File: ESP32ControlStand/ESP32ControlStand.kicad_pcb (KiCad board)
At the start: 2 copper layers, 184.1 x 144.1 mm, 118 parts, among them CON101 BARREL_JACK, J101 Button & LED Panel, J102 Horn, J103 Brake, J104 I2C Display, J105 Button & LED Panel, J106 Light Switch, J107 Reverser, J108 Throttle, J109 On-Off Switch, J401 RJ45, J402 RJ45, P101 CONN_8, P102 Misc buttons, bell, status LED, P106 CONN_3, P107 CONN_3, P201 CONN_5, P301 CONN_5, SW101 A, SW102 B, SW103 C, SW104 D, SW105 Bell, SW201 SW_PUSH_SMALL, SW202 SW_PUSH_SMALL, SW203 SW_PUSH_SMALL, SW204 SW_PUSH_SMALL, SW205 SW_PUSH_SMALL, SW206 SW_PUSH_SMALL, SW207 SW_PUSH_SMALL, SW208 SW_PUSH_SMALL, SW301 SW_PUSH_SMALL, SW302 SW_PUSH_SMALL, SW303 SW_PUSH_SMALL, SW304 SW_PUSH_SMALL, SW305 SW_PUSH_SMALL, SW306 SW_PUSH_SMALL, SW307 SW_PUSH_SMALL, SW308 SW_PUSH_SMALL, T201 Buttons, T202 LEDS, T301 Buttons, T302 LEDS, T401 + 15 in -, T402 + 15 out -, U101 ADAFRUIT_POWERBOOST_500, U102 TTGO-T1, U201 MCP23017, U202 TBD62083A, U301 MCP23017, U302 TBD62083A, U401 TCAN332DR, U402 SN65HVD233-HT, U501 LM2574N-5.0

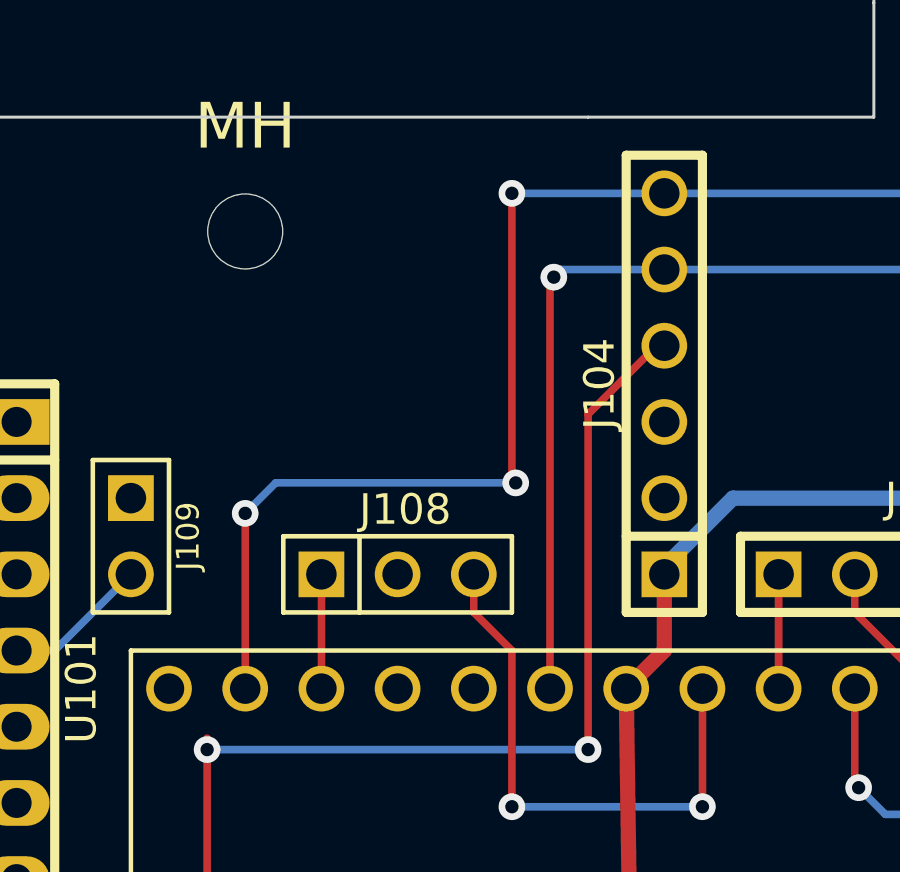
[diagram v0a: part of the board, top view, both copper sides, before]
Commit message: Update circuit to use "Default" SDA/SDL.
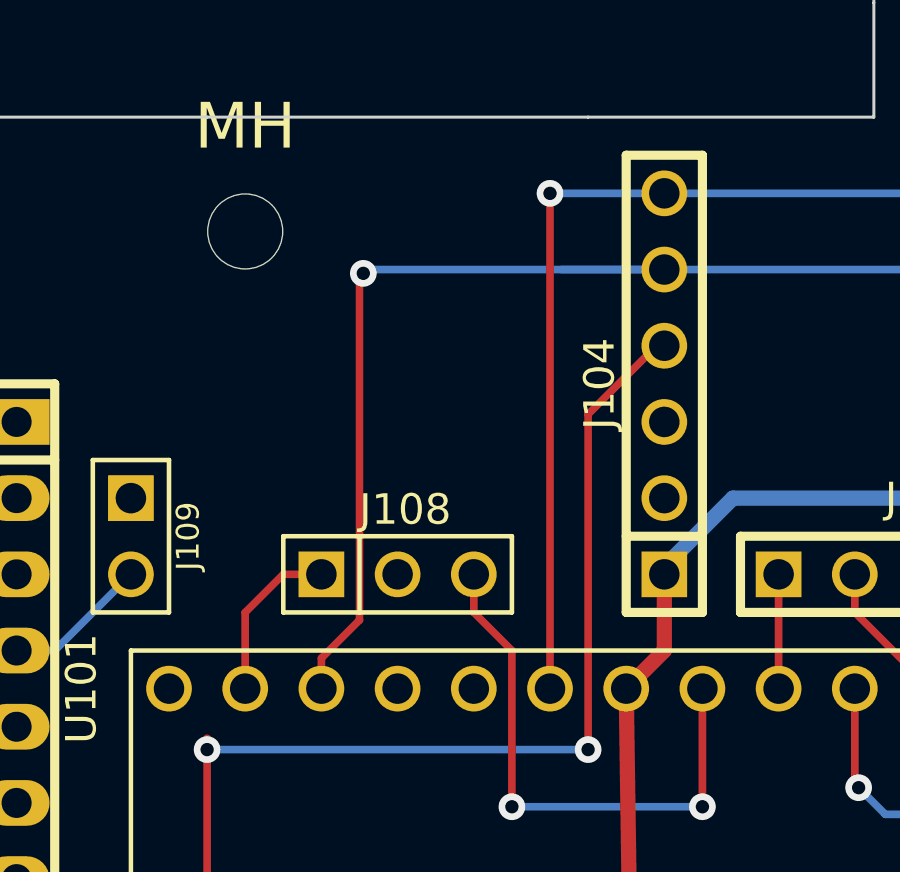
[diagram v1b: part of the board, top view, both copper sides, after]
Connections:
- U102 pad 31: /SCL -> /SDA
- U102 pad 34: /ThrottleA -> /SCL
- U102 pad 35: /SDA -> /ThrottleA
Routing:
- net /SCL: track 42.0 -> 52.1 mm
- net /SDA: track 54.2 -> 44.5 mm, vias 3 -> 1
- net /ThrottleA: track 3.81 -> 5.61 mm

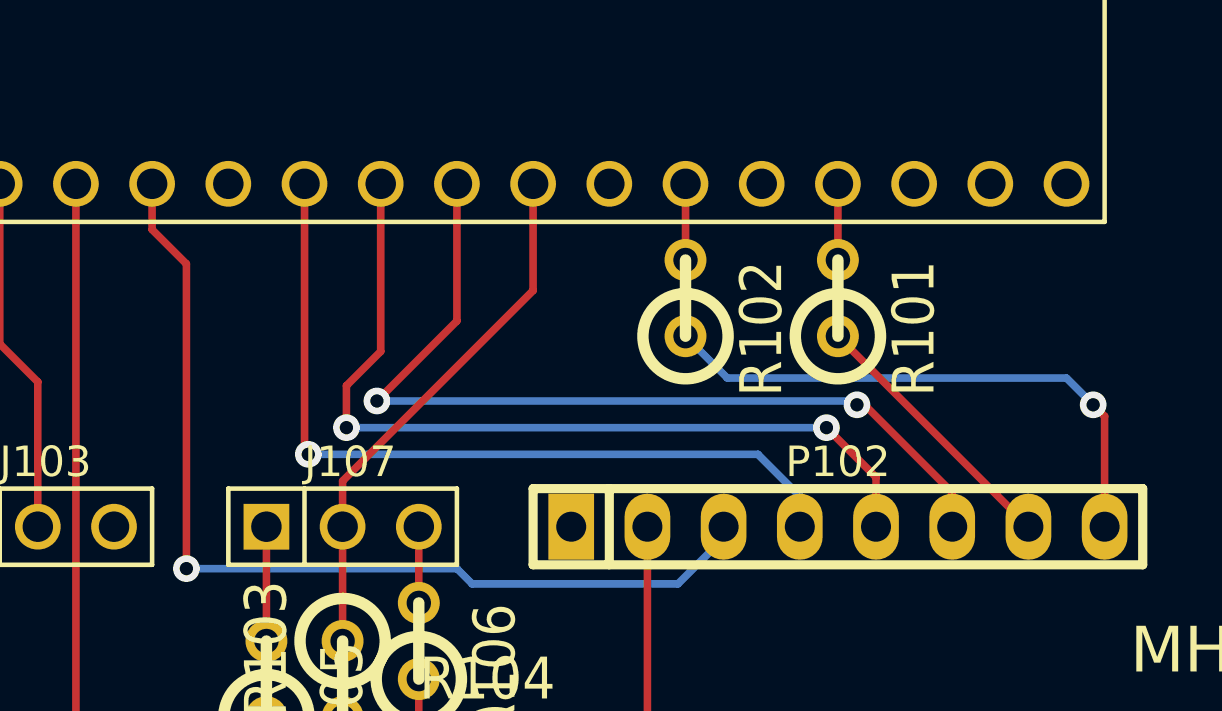
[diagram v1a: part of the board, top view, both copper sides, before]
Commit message: Fix I/O conflict (Status_G).
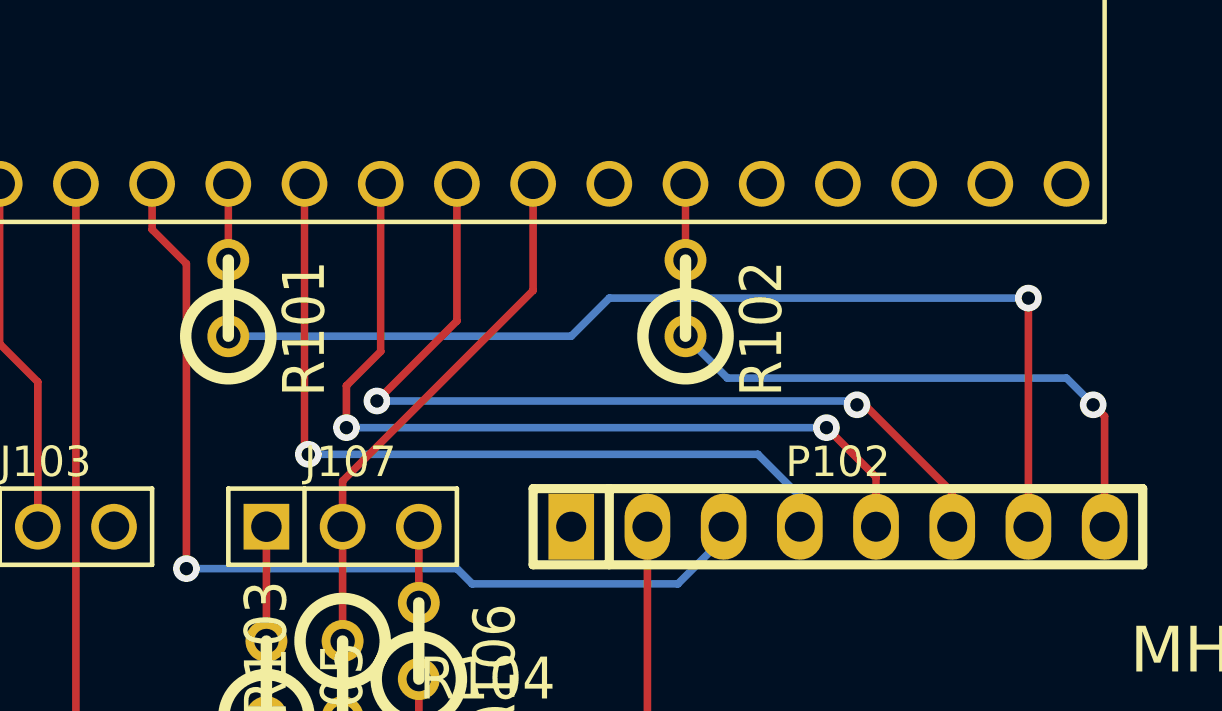
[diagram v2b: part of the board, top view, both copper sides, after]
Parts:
- moved R101 20.3 mm to (191.8, 210.8)
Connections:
- U102 pad 15: /Status_G -> (no net)
- U102 pad 7: (no net) -> /Status_G
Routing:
- net N-0000035: track 8.98 -> 34.8 mm, vias 0 -> 1

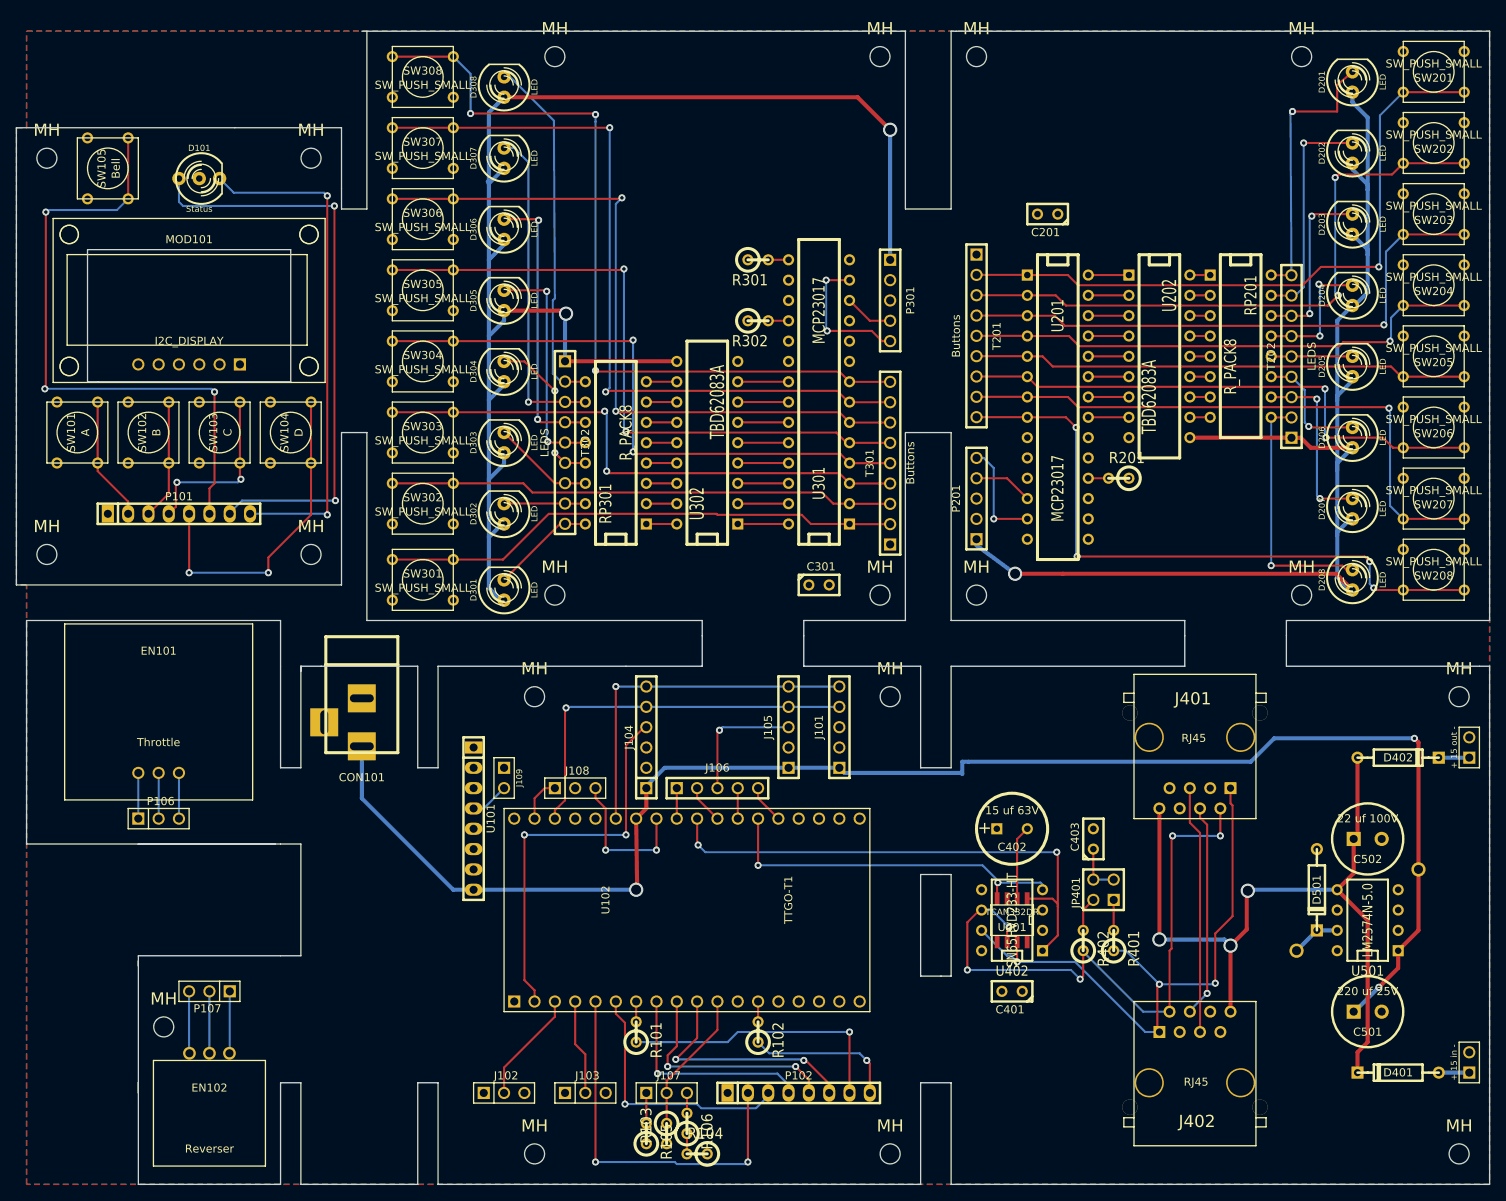
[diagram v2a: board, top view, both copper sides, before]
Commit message: Add I2C pullups.
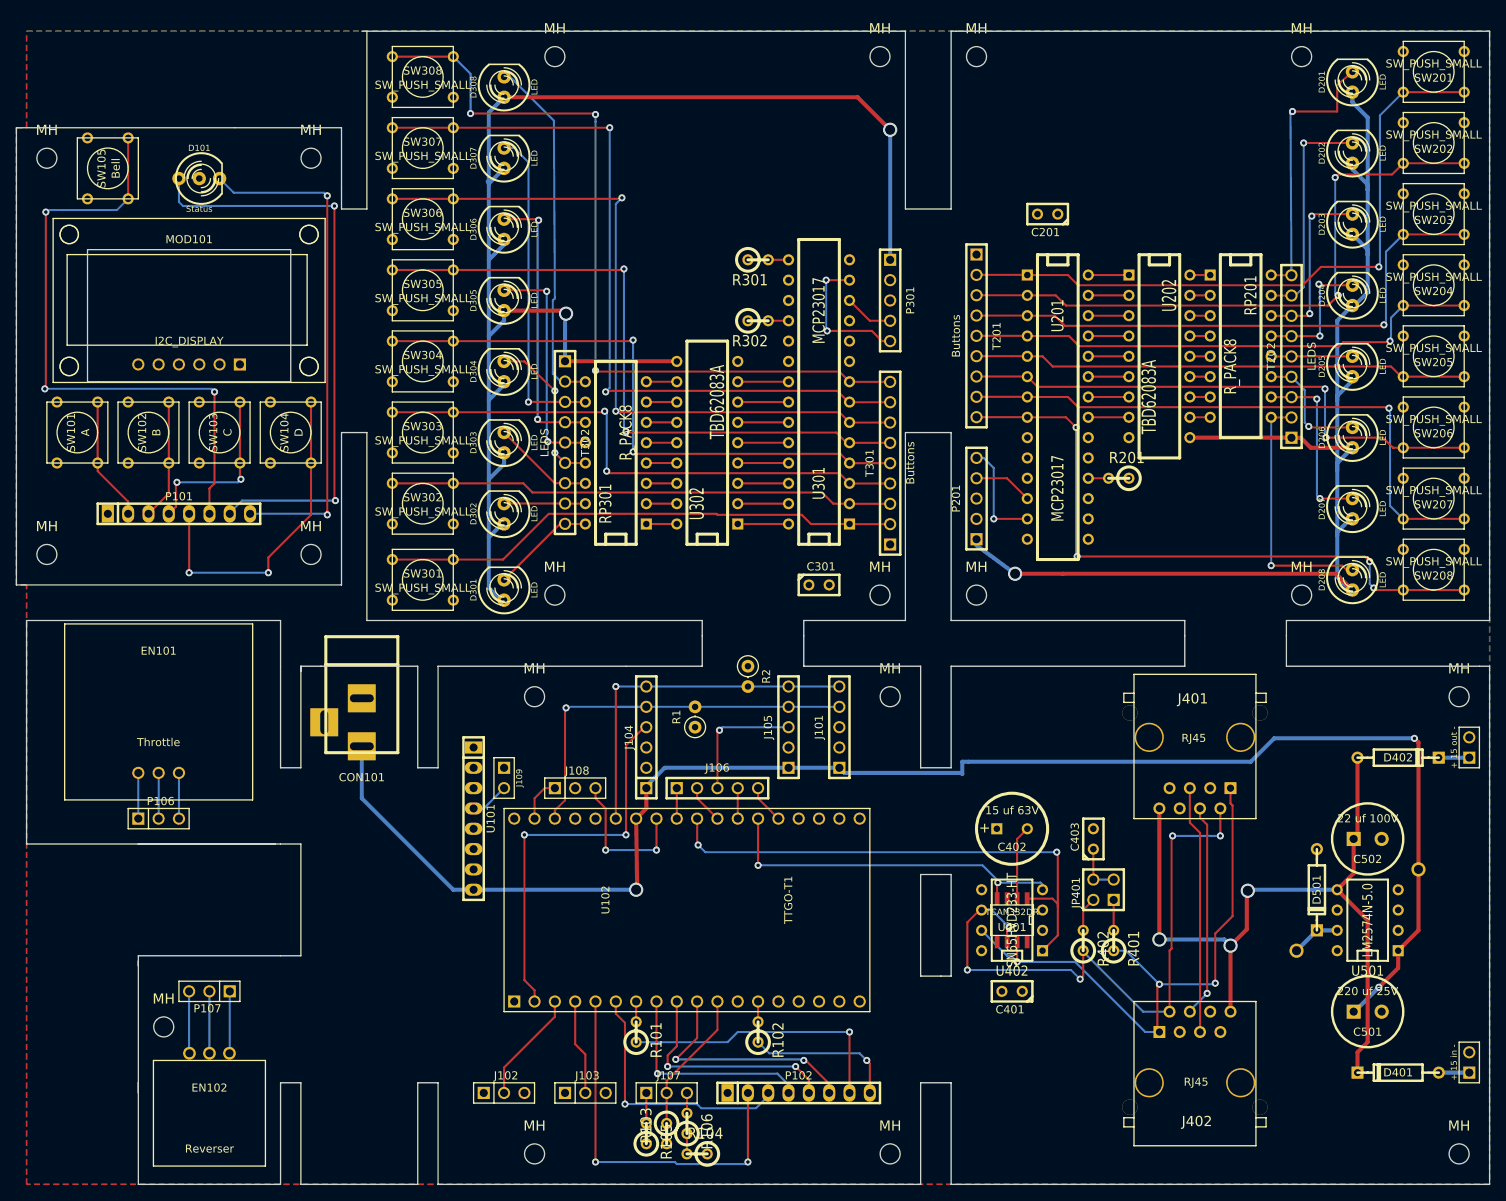
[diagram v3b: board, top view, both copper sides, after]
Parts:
- added R1: 2.4K Ohms, Resistors_THT:R_Axial_DIN0207_L6.3mm_D2.5mm_P2.54mm_Vertical, F.Cu at (199.1, 172.7)
- added R2: 2.4K Ohms, Resistors_THT:R_Axial_DIN0207_L6.3mm_D2.5mm_P2.54mm_Vertical, F.Cu at (205.7, 165.1)
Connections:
- net /CAN Transceiver/CAN_RX renamed /CAN_RX
- net /CAN Transceiver/CAN_TX renamed /CAN_TX
- CON101 pad 3: (no net) -> Net-(CON101-Pad3)
- J104 pad 2: (no net) -> Net-(J104-Pad2)
- U101 pad 1: (no net) -> Net-(U101-Pad1)
- U101 pad 3: (no net) -> Net-(U101-Pad3)
- U101 pad 6: (no net) -> Net-(U101-Pad6)
- U102 pad 12: (no net) -> /SCLK
- U102 pad 15: (no net) -> Net-(U102-Pad15)
- U102 pad 16: (no net) -> Net-(U102-Pad16)
- U102 pad 17: (no net) -> Net-(U102-Pad17)
- U102 pad 18: (no net) -> Net-(U102-Pad18)
- U102 pad 19: (no net) -> Net-(U102-Pad19)
- U102 pad 20: (no net) -> Net-(U102-Pad20)
- U102 pad 21: (no net) -> /MOSI
- U102 pad 22: (no net) -> /MISO
- U102 pad 32: (no net) -> Net-(U102-Pad32)
- U102 pad 33: (no net) -> Net-(U102-Pad33)
- U201 pad 19: (no net) -> Net-(U201-Pad19)
- U201 pad 20: (no net) -> Net-(U201-Pad20)
- U301 pad 19: (no net) -> Net-(U301-Pad19)
- U301 pad 20: (no net) -> Net-(U301-Pad20)
- U401 pad 5: (no net) -> Net-(U401-Pad5)
- U401 pad 8: (no net) -> Net-(U401-Pad8)
